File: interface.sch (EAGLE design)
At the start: 37 parts, among them U1 ATMEGA328P_PDIP

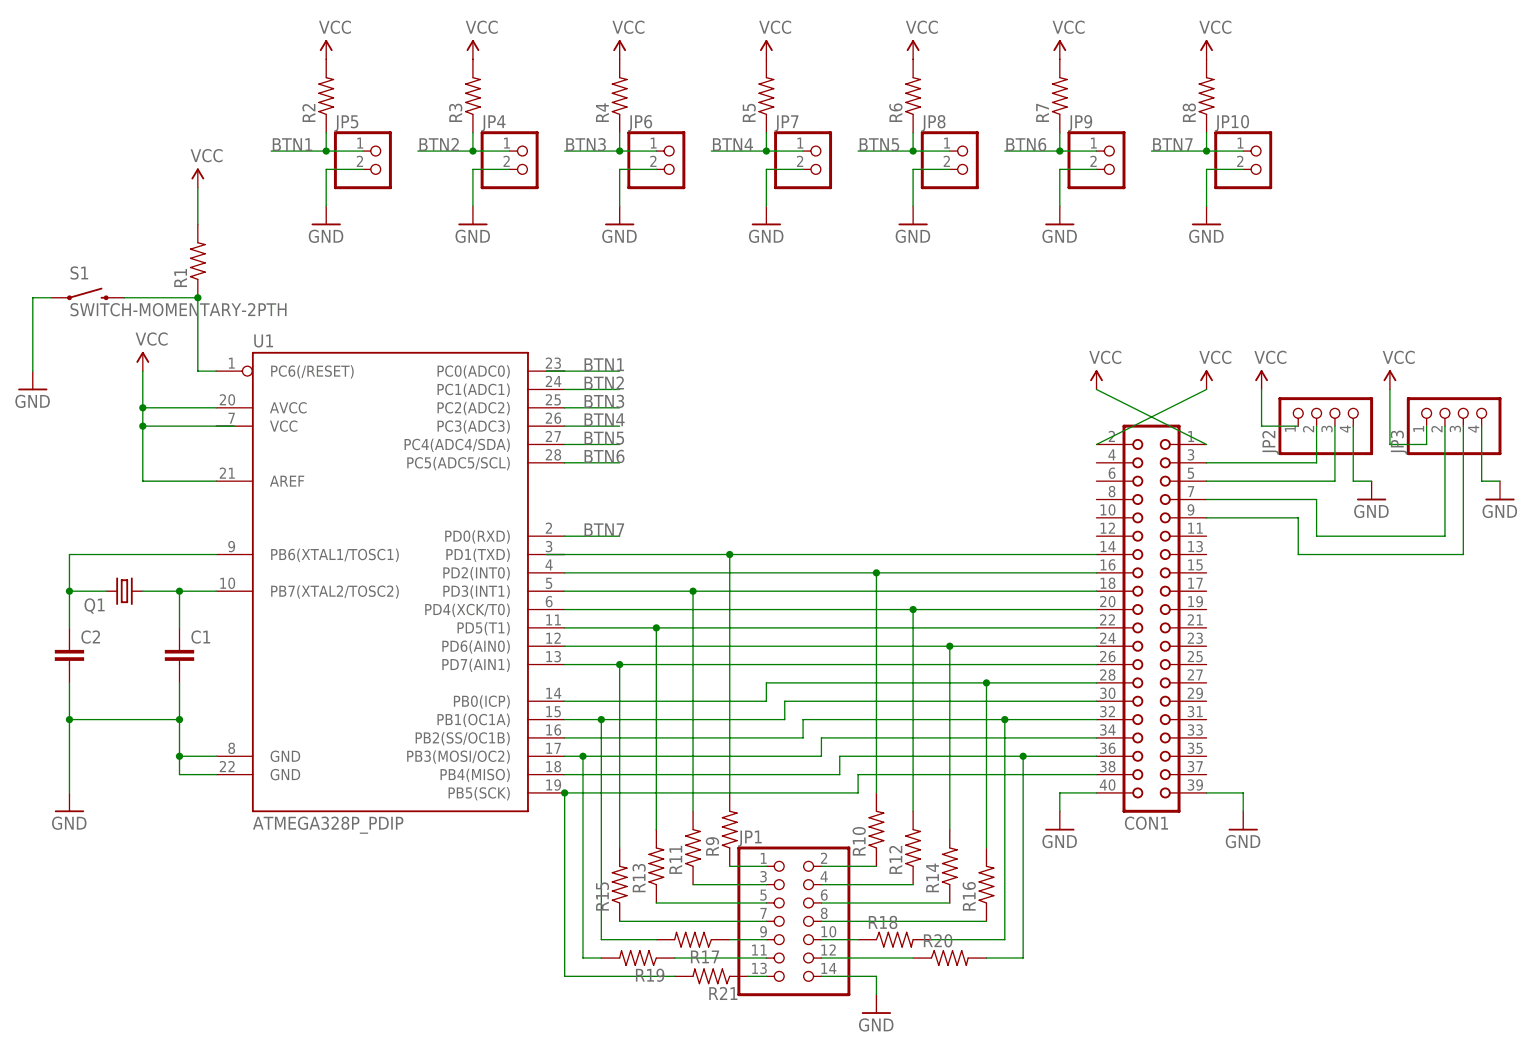
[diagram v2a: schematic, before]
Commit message: Reorg the schematic. First pass at autorouter
Need to check if LED resistors will affect XBox circuitry
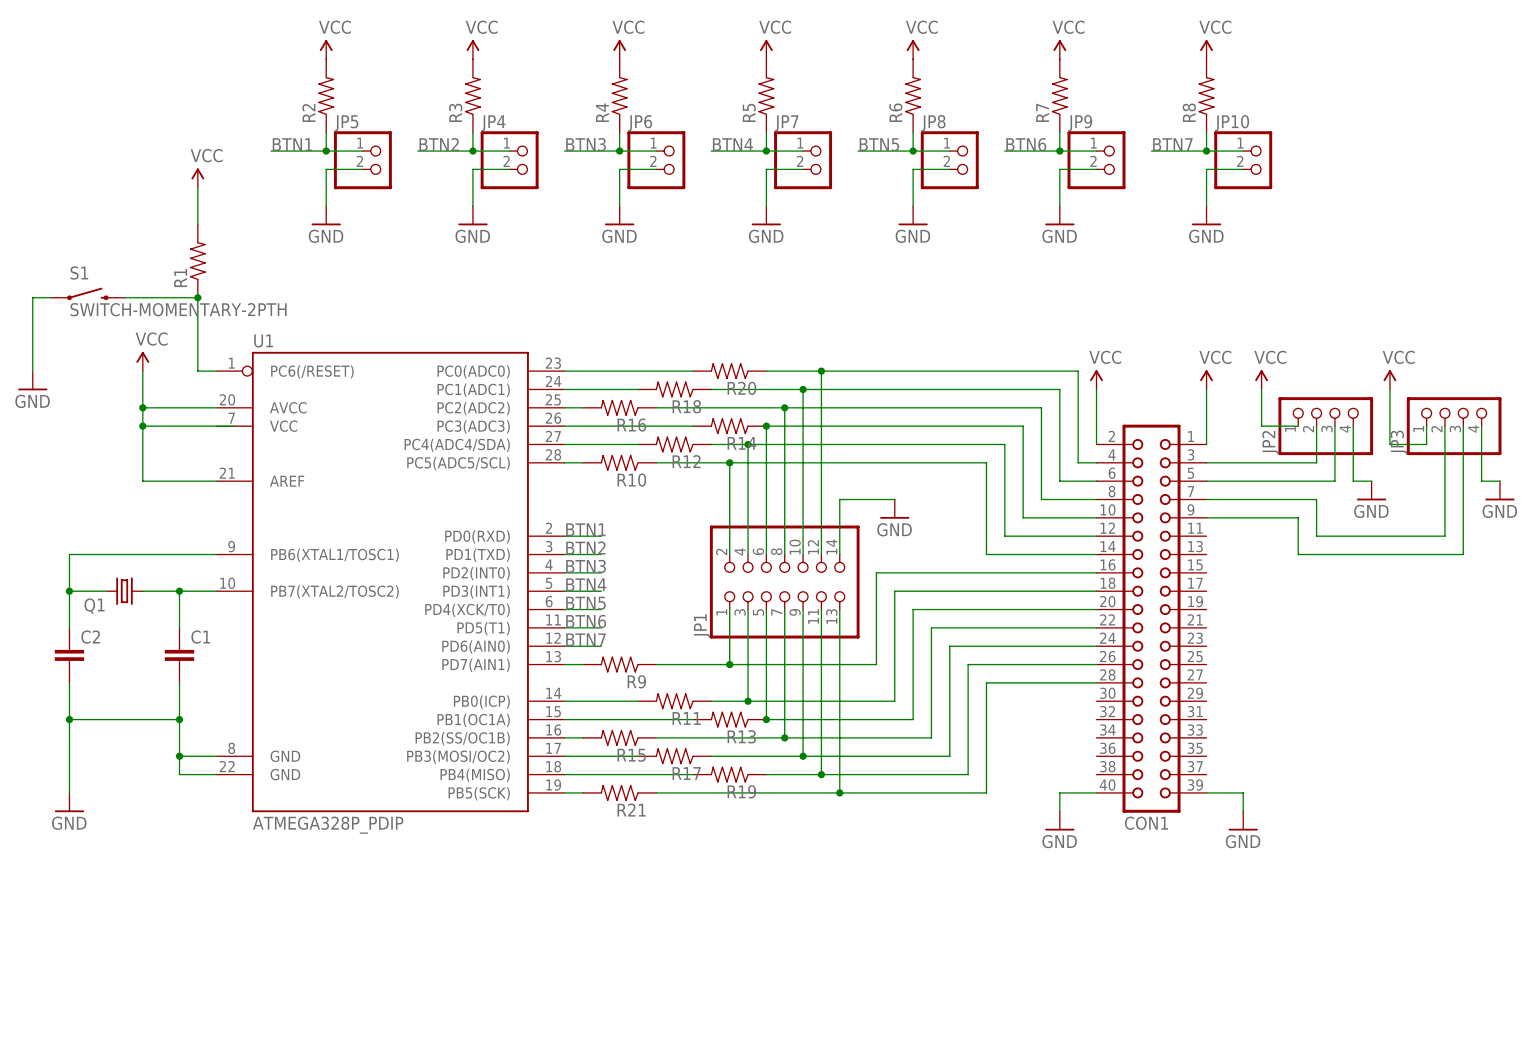
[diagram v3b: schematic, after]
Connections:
- net BTN1: now also U1.PD0(RXD)
- net BTN2: now also U1.PD1(TXD); no longer U1.PC1(ADC1)
- net BTN3: now also U1.PD2(INT0); no longer U1.PC2(ADC2)
- net BTN4: now also U1.PD3(INT1); no longer U1.PC3(ADC3)
- net BTN5: now also U1.PD4(XCK/T0); no longer U1.PC4(ADC4/SDA)
- net BTN6: now also U1.PD5(T1); no longer U1.PC5(ADC5/SCL)
- net BTN7: now also U1.PD6(AIN0); no longer U1.PD0(RXD)
- net N$10: now also U1.PB2(SS/OC1B); no longer CON1.26, U1.PD7(AIN1)
- net N$11: now also CON1.22, JP1.7, R15.1; no longer CON1.24, R14.2, U1.PD6(AIN0)
- net N$12: now also CON1.24, JP1.9, R17.1; no longer CON1.22, R13.2, U1.PD5(T1)
- net N$13: now also R17.2, U1.PB3(MOSI/OC2); no longer CON1.20, R12.2, U1.PD4(XCK/T0)
- net N$14: now also R19.2, U1.PB4(MISO); no longer CON1.18, R11.2, U1.PD3(INT1)
- net N$15: now also R21.2, U1.PB5(SCK); no longer CON1.16, R10.2, U1.PD2(INT0)
- net N$16: now also CON1.28, JP1.13, R21.1; no longer CON1.14, R9.2
- net N$21: now also CON1.26, JP1.11, R19.1; no longer JP1.1, R9.1
- net N$22: now also R10.2, U1.PC5(ADC5/SCL); no longer JP1.2, R10.1
- net N$23: now also CON1.14, JP1.2, R10.1; no longer JP1.3, R11.1
- net N$24: now also R12.2, U1.PC4(ADC4/SDA); no longer JP1.4, R12.1
- net N$25: now also CON1.12, JP1.4, R12.1; no longer JP1.5, R13.1
- net N$26: now also R14.2, U1.PC3(ADC3); no longer JP1.6, R14.1
- net N$27: now also CON1.10, JP1.6, R14.1; no longer JP1.7, R15.1
- net N$28: now also R16.2, U1.PC2(ADC2); no longer JP1.8, R16.1
- net N$29: now also CON1.8, JP1.8, R16.1; no longer JP1.9, R17.1
- net N$30: now also R18.2, U1.PC1(ADC1); no longer JP1.10, R18.1
- net N$31: now also CON1.6, JP1.10, R18.1; no longer JP1.11, R19.1
- net N$32: now also R20.2, U1.PC0(ADC0); no longer JP1.12, R20.1
- net N$33: now also CON1.4, JP1.12, R20.1; no longer JP1.13, R21.1
- net N$4: now also R9.2, U1.PD7(AIN1); no longer CON1.28, R16.2, U1.PB0(ICP)
- net N$5: now also CON1.16, JP1.1, R9.1; no longer CON1.30, R17.2, U1.PB1(OC1A)
- net N$6: now also R11.2, U1.PB0(ICP); no longer CON1.32, R18.2, U1.PB2(SS/OC1B)
- net N$7: now also CON1.18, JP1.3, R11.1; no longer CON1.34, R19.2, U1.PB3(MOSI/OC2)
- net N$8: now also CON1.20, JP1.5, R13.1; no longer CON1.36, R20.2, U1.PB4(MISO)
- net N$9: now also R13.2, U1.PB1(OC1A); no longer CON1.38, R21.2, U1.PB5(SCK)
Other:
- moved on the sheet: JP1, R10, R11, R12, R13, R14, R15, R16, R17, R18, R19, R20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
